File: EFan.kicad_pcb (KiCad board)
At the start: 2 copper layers, 48.9 x 38.1 mm, 46 parts, among them J1 Conn_01x04_Male, J2 Conn_01x03_Male, M1 Fan, Q1 TIP41, SW1 SW_Push, U1 STM32F030F4Px, U2 LM358, U3 MC34063AD

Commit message: refine pcb
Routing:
- net Net-(R11-Pad2): track 20.8 -> 17.4 mm, vias 0 -> 5
- net +28V: track 89.7 -> 91.6 mm
- added copper zone on B.Cu, net Net-(R11-Pad2)

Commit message: production 2
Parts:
- removed R13: 3R3, Resistor_SMD:R_0603_1608Metric_Pad1.05x0.95mm_HandSolder
- removed the REF** at (79.2, 102.5)
- removed the REF** at (104.0, 102.5)
- added C10: 100u, EFan:C_Radial_D5.0mm_H7.0mm_P2.00mm, F.Cu at (103.6, 114.2)
- added C11: 22u, EFan:CP_EIA-3216-18_Kemet-A_Pad1.58x1.35mm_HandSolder, F.Cu at (93.3, 114.4)
- added C9: 104, Capacitor_SMD:C_0603_1608Metric_Pad1.05x0.95mm_HandSolder, F.Cu at (84.8, 91.9)
- added L2: 1u, Inductor_SMD:L_0805_2012Metric_Pad1.15x1.40mm_HandSolder, F.Cu at (103.8, 118.2)
- added REF**: MountingHole_3.2mm_M3, MountingHole:MountingHole_3.2mm_M3, F.Cu at (116.6, 107.8)
- added REF**: MountingHole_3.2mm_M3, MountingHole:MountingHole_3.2mm_M3, F.Cu at (116.6, 129.3)
- added REF**: MountingHole_3.2mm_M3, MountingHole:MountingHole_3.2mm_M3, F.Cu at (116.6, 91.8)
- added TP10: 5V, TestPoint:TestPoint_Loop_D2.50mm_Drill1.0mm, F.Cu at (109.2, 120.0)
- added TP11: 3.3V, TestPoint:TestPoint_Loop_D2.50mm_Drill1.0mm, F.Cu at (109.1, 109.0)
- added TP3: GND, Connector_PinHeader_2.54mm:PinHeader_1x01_P2.54mm_Vertical, F.Cu at (72.0, 129.2)
- added TP4: DAC, TestPoint:TestPoint_Loop_D2.50mm_Drill1.0mm, F.Cu at (81.9, 100.2)
- added TP5: 28V, Connector_PinHeader_2.54mm:PinHeader_1x01_P2.54mm_Vertical, F.Cu at (72.0, 126.6)
- added TP6: FB, TestPoint:TestPoint_Loop_D2.50mm_Drill1.0mm, F.Cu at (81.9, 96.3)
- added TP7: 28V Loop, TestPoint:TestPoint_Loop_D2.50mm_Drill1.0mm, F.Cu at (75.7, 119.4)
- added TP8: GND Loop, TestPoint:TestPoint_Loop_D2.50mm_Drill1.0mm, F.Cu at (75.7, 129.4)
- added TP9: 5VRAW, TestPoint:TestPoint_Loop_D2.50mm_Drill1.0mm, F.Cu at (109.2, 129.4)
- added U4: AMS1117-3.3, Package_TO_SOT_SMD:SOT-223-3_TabPin2, F.Cu at (98.2, 112.8)
- C5: value 220u -> 100u; footprint Capacitor_SMD:CP_Elec_8x10 -> EFan:C_Radial_D5.0mm_H7.0mm_P2.00mm
- C6: value 100u -> 47u; footprint Capacitor_SMD:CP_Elec_8x10 -> EFan:CP_Elec_6.3x5.4
- D1: value SS34 -> SS24
- L1: value 220u -> 1m; footprint EFan:SMD,4.5x4x3.2mm Inductor -> EFan:L_Radial_D7.0mm_P3.00mm
- R11: value 3R3 -> 126k
- R12: value 3R3 -> 143
- R14: value 3R3 -> 2R7
- R15: value 6.8k -> 12k
- R16: value 11k -> 36k
- TH1: value Thermistor_NTC -> NTC
- TP1: value TestPoint -> NTC; footprint Connector_PinHeader_2.54mm:PinHeader_1x01_P2.54mm_Vertical -> TestPoint:TestPoint_Loop_D2.50mm_Drill1.0mm
- TP2: value TestPoint -> TSET; footprint Connector_PinHeader_2.54mm:PinHeader_1x01_P2.54mm_Vertical -> TestPoint:TestPoint_Loop_D2.50mm_Drill1.0mm
- moved C8 39.2 mm to (76.5, 116.7), turned to 0 degrees
- moved R17 38.0 mm to (73.7, 95.2), turned to 270 degrees
- moved Q1 37.8 mm to (78.1, 99.1), turned to 90 degrees
- moved JP1 35.9 mm to (104.6, 109.7)
- moved TH1 33.5 mm to (72.0, 119.0), turned to 0 degrees
- moved R1 30.5 mm to (105.3, 107.7), turned to 180 degrees
- moved R15 29.2 mm to (105.4, 127.5)
- moved U2 25.3 mm to (83.2, 114.3), turned to 180 degrees
- moved SW1 25.2 mm to (105.9, 98.3), turned to 270 degrees
- moved J1 24.6 mm to (72.0, 106.6), turned to 180 degrees
- moved R16 24.4 mm to (105.4, 123.4), turned to 270 degrees
- moved M1 23.3 mm to (72.0, 114.4), turned to 180 degrees
- moved R14 22.7 mm to (83.9, 129.3), turned to 0 degrees
- moved R9 22.1 mm to (82.4, 103.5)
- moved R2 21.0 mm to (99.1, 106.7), turned to 90 degrees
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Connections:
- C5 pad 1: VCC -> Net-(C5-Pad1)
- L1 pad 2: VCC -> Net-(C5-Pad1)
- R11 pad 1: +28V -> Net-(M1-Pad2)
- R11 pad 2: Net-(R11-Pad2) -> Net-(C9-Pad1)
- R12 pad 1: +28V -> Net-(C9-Pad1)
- R12 pad 2: Net-(R11-Pad2) -> GND
- R14 pad 2: Net-(R11-Pad2) -> /Step Down Power/Sensed28
- R16 pad 1: VCC -> Net-(C5-Pad1)
- R17 pad 2: Net-(R17-Pad2) -> /DAC
- TP1 pad 1: GND -> Net-(R7-Pad2)
- TP2 pad 1: +28V -> Net-(R9-Pad2)
- U1 pad 13: Net-(U1-Pad13) -> Net-(C9-Pad1)
- U2 pad 1: Net-(R17-Pad2) -> /DAC
- U2 pad 2: Net-(R17-Pad2) -> /DAC
- U2 pad 5: GND -> /DAC
- U3 pad 1: Net-(R11-Pad2) -> /Step Down Power/Sensed28
- U3 pad 7: Net-(R11-Pad2) -> /Step Down Power/Sensed28
- U3 pad 8: Net-(R11-Pad2) -> /Step Down Power/Sensed28
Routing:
- net +28V: track 91.6 -> 37.4 mm
- net /DAC: track 0.00 -> 34.9 mm
- net /DIP2: track 5.34 -> 34.7 mm, vias 0 -> 2
- net /DIP1: track 4.70 -> 31.2 mm, vias 0 -> 2
- net Net-(C9-Pad1): track 0.00 -> 26.3 mm, vias 0 -> 2
- net Net-(C5-Pad1): track 0.00 -> 24.1 mm
- net Net-(R15-Pad1): track 4.96 -> 28.0 mm, vias 0 -> 2
- net Net-(R7-Pad2): track 16.2 -> 37.1 mm, vias 2 -> 1
- net /SWDIO: track 10.5 -> 30.1 mm, vias 0 -> 2
- net /SWCLK: track 8.22 -> 26.8 mm, vias 0 -> 2
- net /DIP3: track 4.02 -> 22.5 mm
- net Net-(R11-Pad2): track 17.4 -> 0.00 mm, vias 5 -> 0
- net /DIP4: track 8.47 -> 25.7 mm
- net Net-(C1-Pad1): track 15.6 -> 31.4 mm, vias 0 -> 1
- net VCC: track 115.7 -> 101.7 mm, vias 0 -> 2
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- added copper zone on F.Cu, net GND
- removed copper zone on B.Cu, net Net-(R11-Pad2)
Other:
- board size 48.9 x 38.1 mm -> 53.1 x 48.3 mm

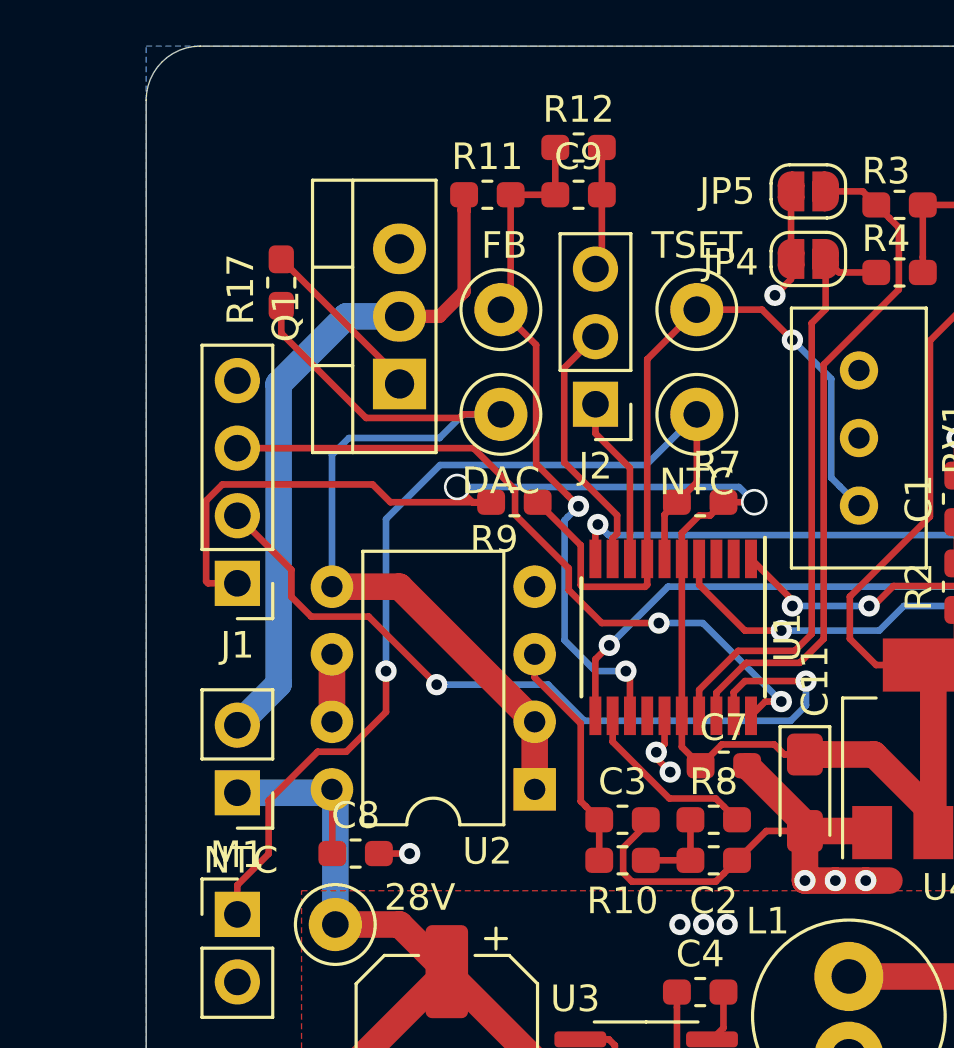
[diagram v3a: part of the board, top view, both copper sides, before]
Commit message: add 2 coupling caps in adc input
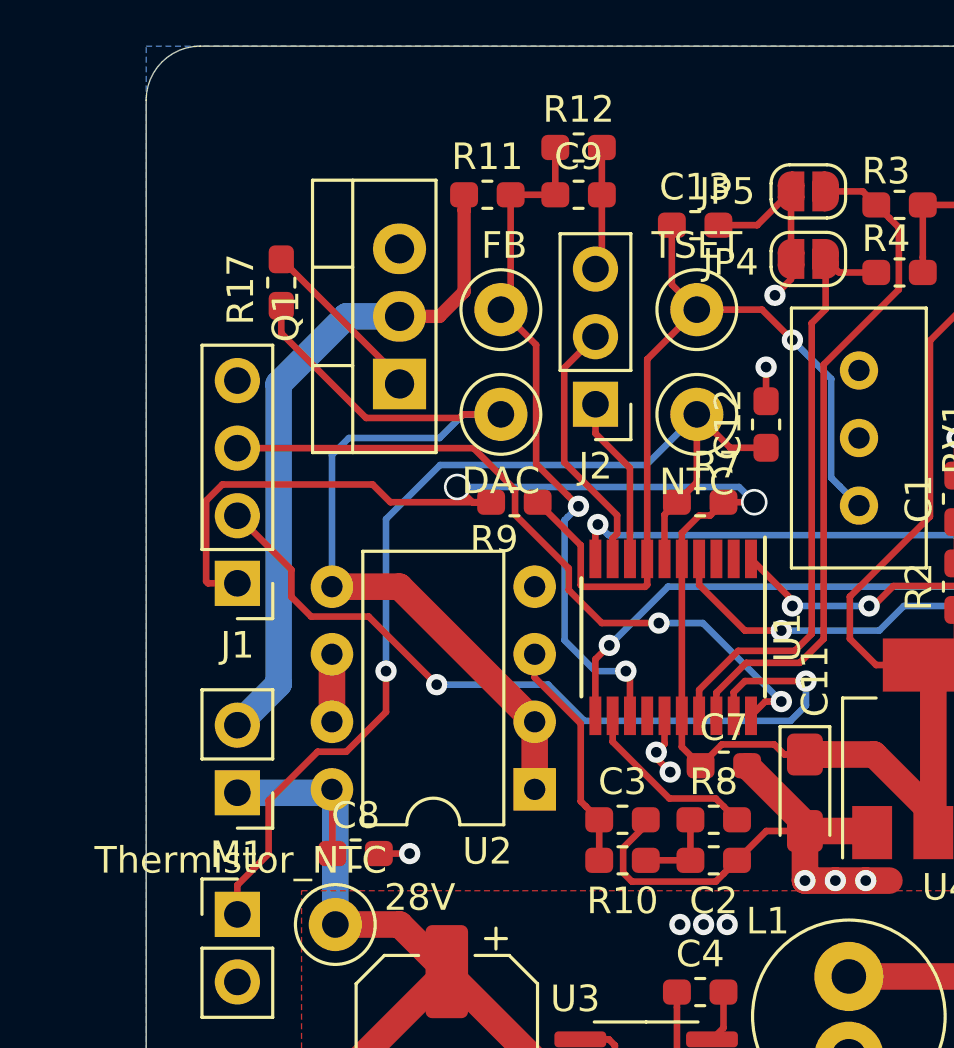
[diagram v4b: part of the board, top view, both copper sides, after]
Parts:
- added C12: 104, Capacitor_SMD:C_0603_1608Metric_Pad1.05x0.95mm_HandSolder, F.Cu at (91.9, 100.6)
- added C13: 104, Capacitor_SMD:C_0603_1608Metric_Pad1.05x0.95mm_HandSolder, F.Cu at (89.2, 93.1)
- R9: value 101 -> 102
- TH1: value NTC -> Thermistor_NTC
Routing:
- net GND: track 71.9 -> 76.4 mm, vias 12 -> 13
- net Net-(C13-Pad1): track 28.8 -> 32.3 mm
- net Net-(C12-Pad1): track 37.1 -> 40.2 mm
